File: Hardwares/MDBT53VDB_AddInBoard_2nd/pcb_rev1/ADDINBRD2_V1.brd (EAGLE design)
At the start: 25 x 31 mm, 21 parts, among them CN1 IF_4PIN, CN2 IF_4PIN, CN3 IF_2PIN, CN4 IF_2PIN, Q1 DMP2035UFDF-7, Q2 BC817-40QA, SW1 SKRPACE010, U1 SN74AHC1G00DRLR, U2 REF3325AIRSER, U3 MCP6232T-E/MNY

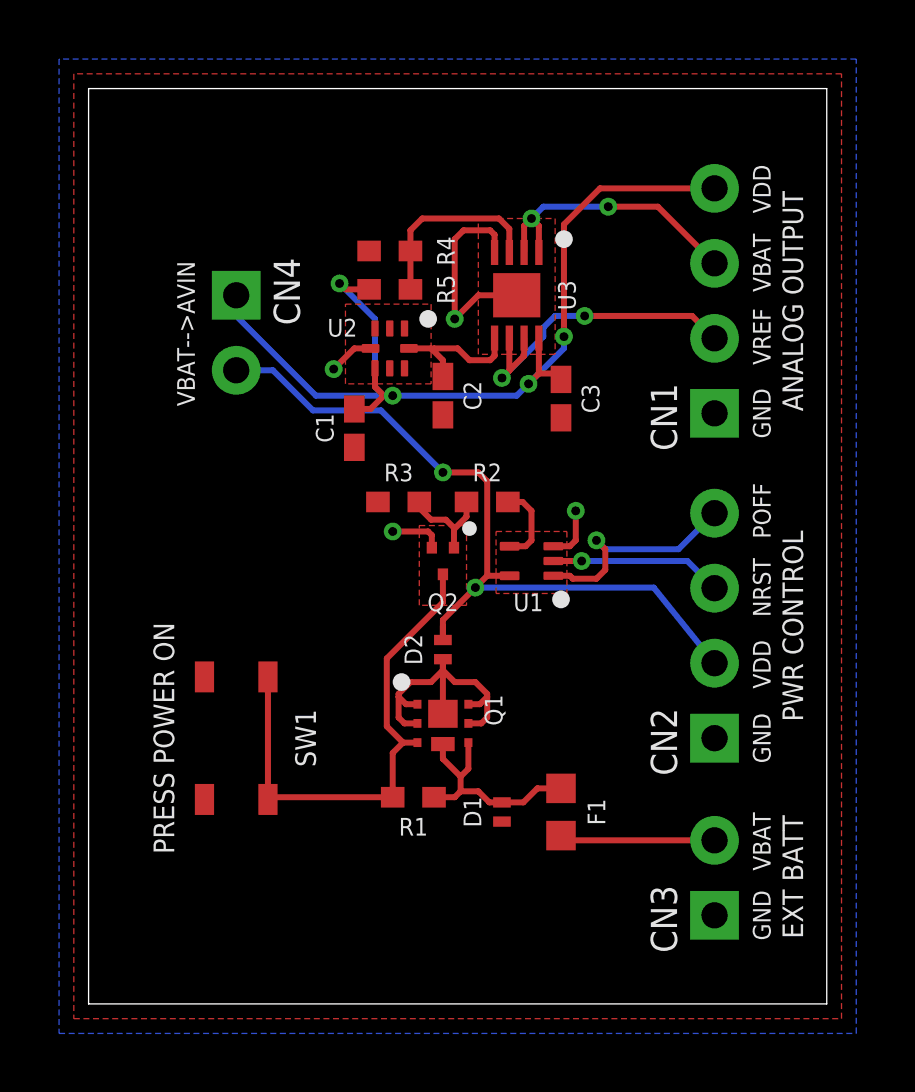
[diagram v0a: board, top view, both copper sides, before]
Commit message: レイアウトを修正
・べたGND領域の調整
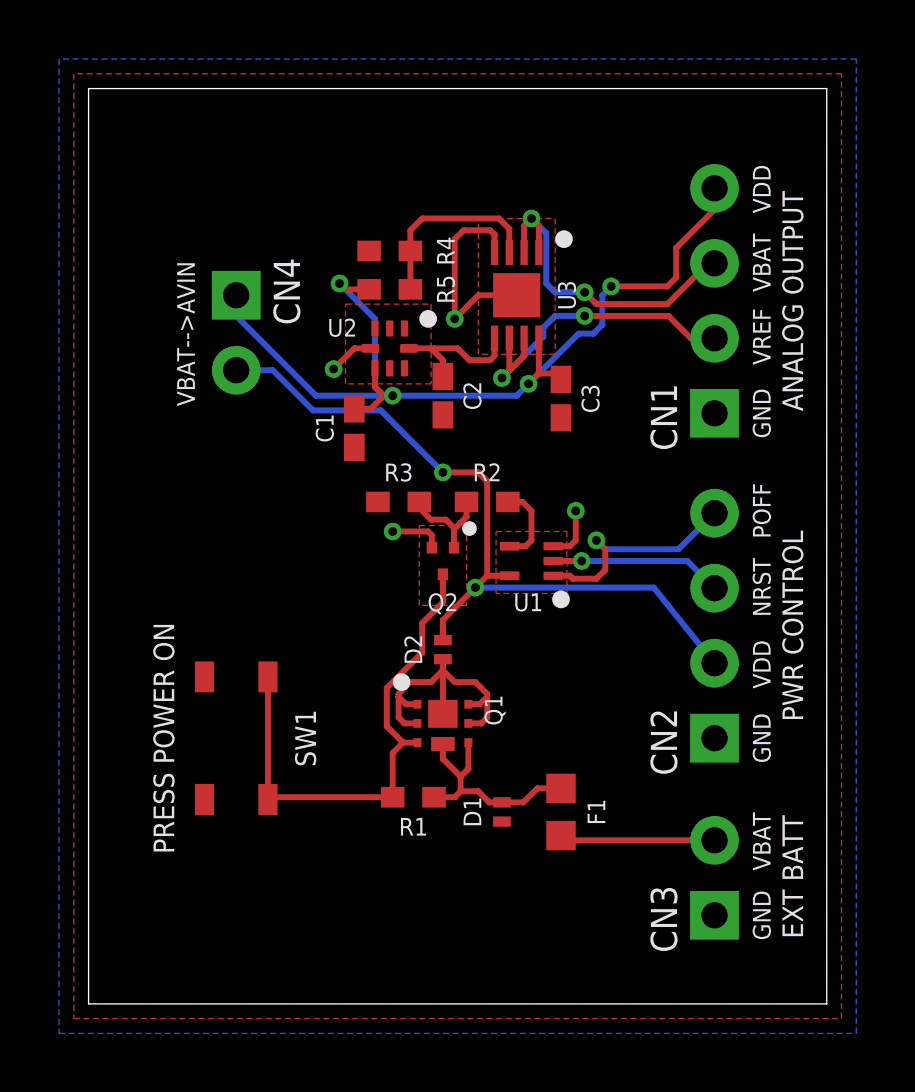
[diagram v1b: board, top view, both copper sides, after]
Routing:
- net AVBAT: track 9.67 -> 11.5 mm
- net AVIN: track 34.3 -> 33.4 mm
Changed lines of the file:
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@@
 <wire x1="11.137" y1="8.85" x2="10.65" y2="8.85" width="0.2032" layer="1"/>
 <wire x1="10.65" y1="8.85" x2="10.1" y2="9.4" width="0.2032" layer="1"/>
-<wire x1="10.1" y1="9.4" x2="10.1" y2="11.7" width="0.2032" layer="1"/>
 <wire x1="10.65" y1="8.85" x2="10.3" y2="8.5" width="0.2032" layer="1"/>
 <wire x1="10.3" y1="7" x2="10.3" y2="8.5" width="0.2032" layer="1"/>
-<wire x1="10.1" y1="11.7" x2="12" y2="13.6" width="0.2032" layer="1"/>
 <wire x1="12" y1="13.6" x2="12" y2="14.55" width="0.2032" layer="1"/>
+<wire x1="10.1" y1="9.4" x2="10.1" y2="10.7" width="0.2032" layer="1"/>
+<wire x1="10.1" y1="10.7" x2="11.3" y2="11.9" width="0.2032" layer="1"/>
+<wire x1="12" y1="13.6" x2="11.3" y2="12.9" width="0.2032" layer="1"/>
+<wire x1="11.3" y1="12.9" x2="11.3" y2="11.9" width="0.2032" layer="1"/>
 </signal>
 <signal name="VIN">
@@
 <wire x1="14.75" y1="25.45" x2="14.75" y2="26.35" width="0.2032" layer="1"/>
 <wire x1="14.75" y1="26.35" x2="15" y2="26.6" width="0.2032" layer="1"/>
-<via x="17.6" y="27" extent="1-16" drill="0.3"/>
-<wire x1="21.2" y1="25.08" x2="19.28" y2="27" width="0.2032" layer="1"/>
-<wire x1="19.28" y1="27" x2="17.6" y2="27" width="0.2032" layer="1"/>
-<wire x1="17.6" y1="27" x2="15.4" y2="27" width="0.2032" layer="16"/>
-<wire x1="15.4" y1="27" x2="15" y2="26.6" width="0.2032" layer="16"/>
+<via x="16.8" y="24.1" extent="1-16" drill="0.3"/>
+<wire x1="15.5" y1="26.1" x2="15" y2="26.6" width="0.2032" layer="16"/>
+<wire x1="16.8" y1="24.1" x2="17.2" y2="23.7" width="0.2032" layer="1"/>
+<wire x1="17.2" y1="23.7" x2="19.6" y2="23.7" width="0.2032" layer="1"/>
+<wire x1="19.6" y1="23.7" x2="20.98" y2="25.08" width="0.2032" layer="1"/>
+<wire x1="21.2" y1="25.08" x2="20.98" y2="25.08" width="0.2032" layer="1"/>
+<wire x1="15.5" y1="26.1" x2="15.5" y2="24.4" width="0.2032" layer="16"/>
+<wire x1="15.5" y1="24.4" x2="15.8" y2="24.1" width="0.2032" layer="16"/>
+<wire x1="15.8" y1="24.1" x2="16.8" y2="24.1" width="0.2032" layer="16"/>
 </signal>
 <signal name="AVREF">
@@
 <via x="16.8" y="23.3" extent="1-16" drill="0.3"/>
 <wire x1="15.8" y1="23.3" x2="16.8" y2="23.3" width="0.2032" layer="16"/>
-<wire x1="21.2" y1="22.54" x2="20.44" y2="23.3" width="0.2032" layer="1"/>
-<wire x1="20.44" y1="23.3" x2="16.8" y2="23.3" width="0.2032" layer="1"/>
+<wire x1="19.64" y1="23.3" x2="16.8" y2="23.3" width="0.2032" layer="1"/>
+<wire x1="21.2" y1="22.54" x2="20.4" y2="22.54" width="0.2032" layer="1"/>
+<wire x1="20.4" y1="22.54" x2="19.64" y2="23.3" width="0.2032" layer="1"/>
 </signal>
 <signal name="AVIN">
@@
 <wire x1="15.25" y1="21.35" x2="15.8" y2="21.35" width="0.2032" layer="1"/>
 <wire x1="15.8" y1="21.35" x2="16" y2="21.15" width="0.2032" layer="1"/>
-<via x="16.1" y="22.6" extent="1-16" drill="0.3"/>
-<wire x1="16.1" y1="22.2" x2="14.9" y2="21" width="0.2032" layer="16"/>
-<wire x1="16.1" y1="22.2" x2="16.1" y2="22.6" width="0.2032" layer="16"/>
-<wire x1="21.2" y1="27.62" x2="17.32" y2="27.62" width="0.2032" layer="1"/>
-<wire x1="17.32" y1="27.62" x2="16.1" y2="26.4" width="0.2032" layer="1"/>
-<wire x1="16.1" y1="26.4" x2="16.1" y2="22.6" width="0.2032" layer="1"/>
+<via x="17.7" y="24.3" extent="1-16" drill="0.3"/>
+<wire x1="16.6" y1="22.7" x2="14.9" y2="21" width="0.2032" layer="16"/>
+<wire x1="21.2" y1="27.62" x2="21.2" y2="26.9" width="0.2032" layer="1"/>
+<wire x1="16.6" y1="22.7" x2="17.1" y2="22.7" width="0.2032" layer="16"/>
+<wire x1="17.1" y1="22.7" x2="17.4" y2="23" width="0.2032" layer="16"/>
+<wire x1="17.4" y1="23" x2="17.4" y2="24" width="0.2032" layer="16"/>
+<wire x1="17.4" y1="24" x2="17.7" y2="24.3" width="0.2032" layer="16"/>
+<wire x1="17.7" y1="24.3" x2="19.6" y2="24.3" width="0.2032" layer="1"/>
+<wire x1="19.6" y1="24.3" x2="19.9" y2="24.6" width="0.2032" layer="1"/>
+<wire x1="19.9" y1="24.6" x2="19.9" y2="25.6" width="0.2032" layer="1"/>
+<wire x1="21.2" y1="26.9" x2="19.9" y2="25.6" width="0.2032" layer="1"/>
 </signal>
 <signal name="N$4">
